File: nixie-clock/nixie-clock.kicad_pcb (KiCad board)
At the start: 2 copper layers, 57 parts, among them J1 Barrel_Jack_Switch, J2 Conn_01x08, J3 Conn_01x06, J4 AVR-ISP-6, U1 NCH6100HV, U10 74HC595, U11 74141, U12 74141, U2 ATmega328P-PU, U3 Mini360_Buck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

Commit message: Placed parts on board in approximate final locations. Created trace breakout for nixie tubes.
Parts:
- removed the REF** at (269.0, 39.0)
- removed the REF** at (254.0, 32.0)
- removed the REF** at (245.0, 37.0)
- removed the REF** at (257.0, 43.0)
- added REF**: MountingHole_2.7mm_M2.5_Pad, MountingHole:MountingHole_2.7mm_M2.5_Pad, F.Cu at (231.0, 46.0)
- added REF**: MountingHole_2.7mm_M2.5_Pad, MountingHole:MountingHole_2.7mm_M2.5_Pad, F.Cu at (240.0, 46.0)
- added REF**: MountingHole_2.7mm_M2.5_Pad, MountingHole:MountingHole_2.7mm_M2.5_Pad, F.Cu at (240.0, 38.0)
- added REF**: MountingHole_2.7mm_M2.5_Pad, MountingHole:MountingHole_2.7mm_M2.5_Pad, F.Cu at (231.0, 54.0)
- moved REF** 213.8 mm to (32.0, 34.0)
- moved N7 150.1 mm to (166.0, 103.0), turned to 180 degrees
- moved R11 137.3 mm to (79.0, 58.5), turned to 270 degrees
- moved R12 130.6 mm to (69.0, 58.5), turned to 270 degrees
- moved R13 127.5 mm to (64.0, 58.5), turned to 270 degrees
- moved R10 126.7 mm to (84.0, 58.5), turned to 270 degrees
- moved R14 126.2 mm to (54.0, 58.5), turned to 270 degrees
- moved R3 122.0 mm to (59.0, 58.5), turned to 270 degrees
- moved R2 120.8 mm to (74.0, 58.5), turned to 270 degrees
- moved R15 119.7 mm to (49.0, 58.5), turned to 270 degrees
- moved N8 114.9 mm to (114.0, 103.0), turned to 180 degrees
- moved C9 103.2 mm to (50.0, 80.0), turned to 90 degrees
- moved U12 100.9 mm to (72.0, 86.0)
- moved U10 97.5 mm to (72.0, 74.0)
- moved J3 90.2 mm to (94.0, 49.0), turned to 180 degrees
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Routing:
- net Net-(N6-Pad1): track 0.00 -> 50.9 mm
- net Net-(N5-Pad1): track 0.00 -> 50.9 mm
- net Net-(N6-Pad0): track 0.00 -> 42.0 mm
- net Net-(N5-Pad0): track 0.00 -> 42.0 mm
- net Net-(N6-Pad2): track 0.00 -> 41.9 mm
- net Net-(N5-Pad2): track 0.00 -> 41.9 mm
- net Net-(N6-Pad3): track 0.00 -> 31.9 mm
- net Net-(N5-Pad3): track 0.00 -> 31.9 mm
- net Net-(N6-Pad9): track 0.00 -> 31.5 mm
- net Net-(N5-Pad9): track 0.00 -> 31.5 mm
- net Net-(N4-Pad1): track 0.00 -> 26.5 mm
- net Net-(N3-Pad1): track 0.00 -> 26.5 mm
- net Net-(N6-Pad8): track 0.00 -> 24.4 mm
- net Net-(N5-Pad8): track 0.00 -> 24.4 mm
- net Net-(N2-Pad1): track 0.00 -> 22.7 mm
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- added copper zone on F.Cu, net +5V
- added copper zone on B.Cu, net GND
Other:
- board outline added: 184 x 112 mm
- net class Default: via_dia 0.8 -> 0.381; via_drill 0.4 -> 0.254
- rule via_min_size: 0.3 -> 0.381

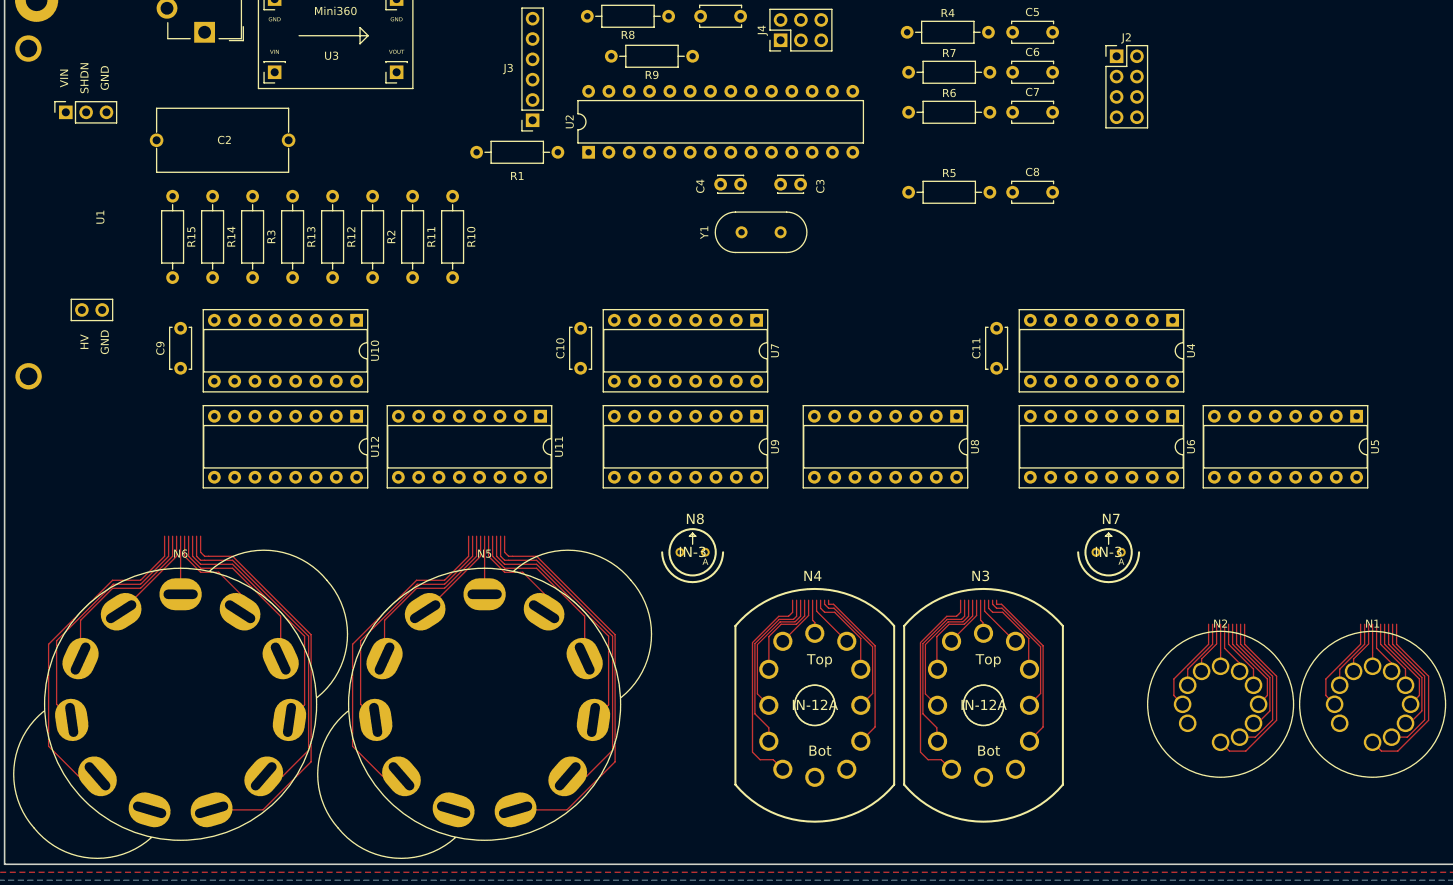
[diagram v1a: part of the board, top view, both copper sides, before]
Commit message: Readded pushbuttons to mainboard as an option. Beginning K155ID1-nixie exchange zone.
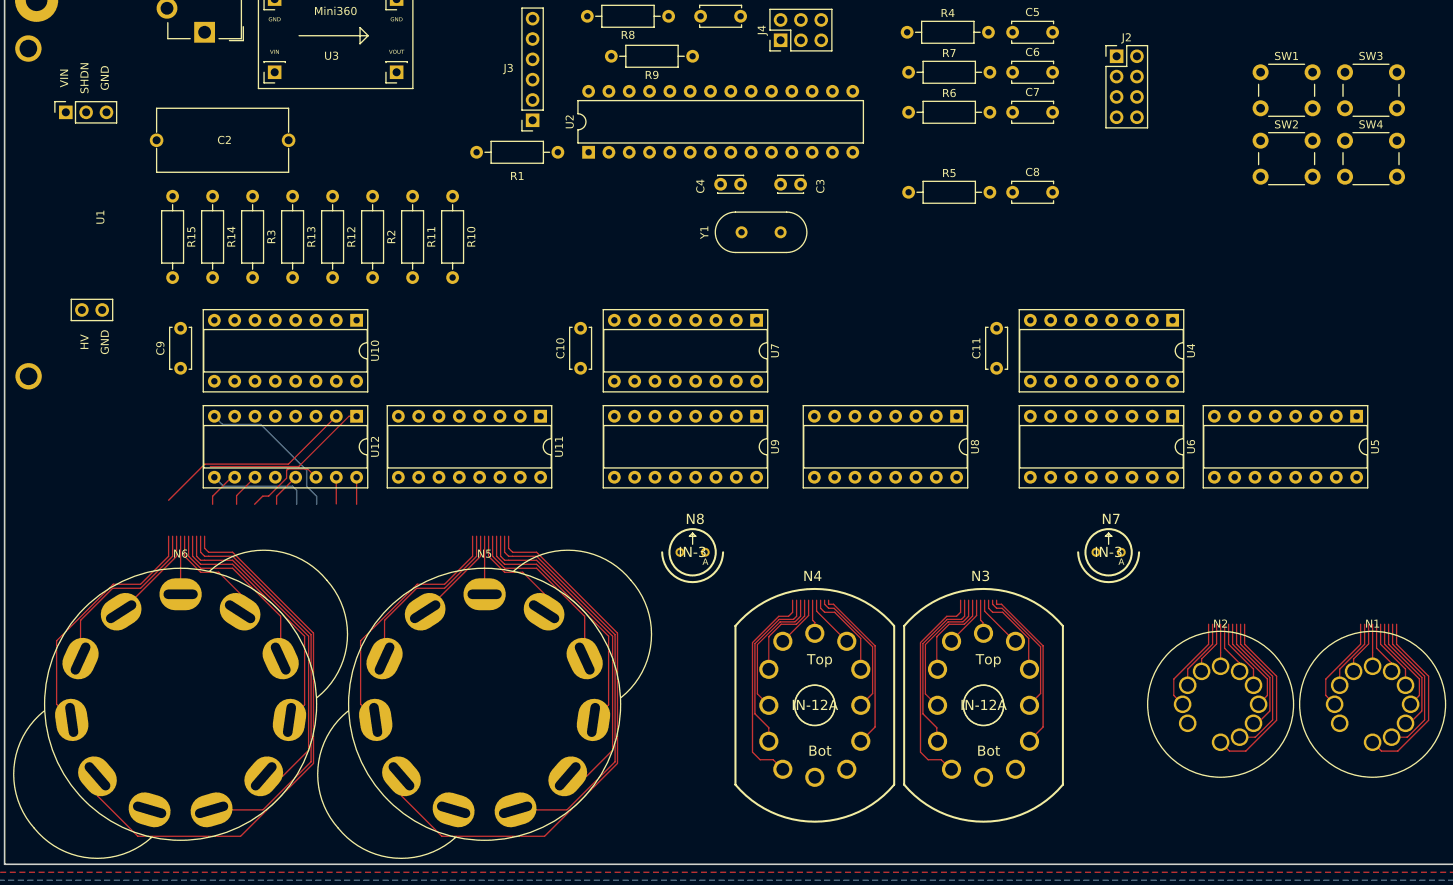
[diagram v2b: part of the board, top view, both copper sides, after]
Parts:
- added SW1: SW_Push, Button_Switch_THT:SW_PUSH_6mm, F.Cu at (185.0, 43.0)
- added SW2: SW_Push, Button_Switch_THT:SW_PUSH_6mm, F.Cu at (185.0, 51.5)
- added SW3: SW_Push, Button_Switch_THT:SW_PUSH_6mm, F.Cu at (195.6, 43.0)
- added SW4: SW_Push, Button_Switch_THT:SW_PUSH_6mm, F.Cu at (195.6, 51.5)
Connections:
- net Net-(N1-Pad0) renamed /shiftout/N1_0
- net Net-(N1-Pad1) renamed /shiftout/N1_1
- net Net-(N1-Pad2) renamed /shiftout/N1_2
- net Net-(N1-Pad3) renamed /shiftout/N1_3
- net Net-(N1-Pad4) renamed /shiftout/N1_4
- net Net-(N1-Pad5) renamed /shiftout/N1_5
- net Net-(N1-Pad6) renamed /shiftout/N1_6
- net Net-(N1-Pad7) renamed /shiftout/N1_7
- net Net-(N1-Pad8) renamed /shiftout/N1_8
- net Net-(N1-Pad9) renamed /shiftout/N1_9
- net Net-(N2-Pad0) renamed /shiftout/N2_0
- net Net-(N2-Pad1) renamed /shiftout/N2_1
- net Net-(N2-Pad2) renamed /shiftout/N2_2
- net Net-(N2-Pad3) renamed /shiftout/N2_3
- net Net-(N2-Pad4) renamed /shiftout/N2_4
- net Net-(N2-Pad5) renamed /shiftout/N2_5
- net Net-(N2-Pad6) renamed /shiftout/N2_6
- net Net-(N2-Pad7) renamed /shiftout/N2_7
- net Net-(N2-Pad8) renamed /shiftout/N2_8
- net Net-(N2-Pad9) renamed /shiftout/N2_9
- net Net-(N3-Pad0) renamed /shiftout/N3_0
- net Net-(N3-Pad1) renamed /shiftout/N3_1
- net Net-(N3-Pad2) renamed /shiftout/N3_2
- net Net-(N3-Pad3) renamed /shiftout/N3_3
- net Net-(N3-Pad4) renamed /shiftout/N3_4
- net Net-(N3-Pad5) renamed /shiftout/N3_5
- net Net-(N3-Pad6) renamed /shiftout/N3_6
- net Net-(N3-Pad7) renamed /shiftout/N3_7
- net Net-(N3-Pad8) renamed /shiftout/N3_8
- net Net-(N3-Pad9) renamed /shiftout/N3_9
- net Net-(N4-Pad0) renamed /shiftout/N4_0
- net Net-(N4-Pad1) renamed /shiftout/N4_1
- net Net-(N4-Pad2) renamed /shiftout/N4_2
- net Net-(N4-Pad3) renamed /shiftout/N4_3
- net Net-(N4-Pad4) renamed /shiftout/N4_4
- net Net-(N4-Pad5) renamed /shiftout/N4_5
- net Net-(N4-Pad6) renamed /shiftout/N4_6
- net Net-(N4-Pad7) renamed /shiftout/N4_7
- net Net-(N4-Pad8) renamed /shiftout/N4_8
- net Net-(N4-Pad9) renamed /shiftout/N4_9
- net Net-(N5-Pad0) renamed /shiftout/N5_0
- net Net-(N5-Pad1) renamed /shiftout/N5_1
- net Net-(N5-Pad2) renamed /shiftout/N5_2
- net Net-(N5-Pad3) renamed /shiftout/N5_3
- net Net-(N5-Pad4) renamed /shiftout/N5_4
- net Net-(N5-Pad5) renamed /shiftout/N5_5
- net Net-(N5-Pad6) renamed /shiftout/N5_6
- net Net-(N5-Pad7) renamed /shiftout/N5_7
- net Net-(N5-Pad8) renamed /shiftout/N5_8
- net Net-(N5-Pad9) renamed /shiftout/N5_9
- net Net-(N6-Pad0) renamed /shiftout/N6_0
- net Net-(N6-Pad1) renamed /shiftout/N6_1
- net Net-(N6-Pad2) renamed /shiftout/N6_2
- net Net-(N6-Pad3) renamed /shiftout/N6_3
- net Net-(N6-Pad4) renamed /shiftout/N6_4
- net Net-(N6-Pad5) renamed /shiftout/N6_5
- net Net-(N6-Pad6) renamed /shiftout/N6_6
- net Net-(N6-Pad7) renamed /shiftout/N6_7
- net Net-(N6-Pad8) renamed /shiftout/N6_8
- net Net-(N6-Pad9) renamed /shiftout/N6_9
- net Net-(U10-Pad1) renamed /shiftout/N5_B
- net Net-(U10-Pad15) renamed /shiftout/N5_A
- net Net-(U10-Pad2) renamed /shiftout/N5_C
- net Net-(U10-Pad3) renamed /shiftout/N5_D
- net Net-(U10-Pad4) renamed /shiftout/N6_A
- net Net-(U10-Pad5) renamed /shiftout/N6_B
- net Net-(U10-Pad6) renamed /shiftout/N6_C
- net Net-(U10-Pad7) renamed /shiftout/N6_D
- net Net-(U4-Pad1) renamed /shiftout/N1_B
- net Net-(U4-Pad15) renamed /shiftout/N1_A
- net Net-(U4-Pad2) renamed /shiftout/N1_C
- net Net-(U4-Pad3) renamed /shiftout/N1_D
- net Net-(U4-Pad4) renamed /shiftout/N2_A
- net Net-(U4-Pad5) renamed /shiftout/N2_B
- net Net-(U4-Pad6) renamed /shiftout/N2_C
- net Net-(U4-Pad7) renamed /shiftout/N2_D
- net Net-(U7-Pad1) renamed /shiftout/N3_B
- net Net-(U7-Pad15) renamed /shiftout/N3_A
- net Net-(U7-Pad2) renamed /shiftout/N3_C
- net Net-(U7-Pad3) renamed /shiftout/N3_D
- net Net-(U7-Pad4) renamed /shiftout/N4_A
- net Net-(U7-Pad5) renamed /shiftout/N4_B
- net Net-(U7-Pad6) renamed /shiftout/N4_C
- net Net-(U7-Pad7) renamed /shiftout/N4_D
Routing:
- net /shiftout/N6_0: track 42.0 -> 74.5 mm
- net /shiftout/N5_0: track 42.0 -> 68.7 mm
- net /shiftout/N6_9: track 31.5 -> 56.9 mm
- net /shiftout/N6_8: track 24.4 -> 45.3 mm
- net /shiftout/N6_2: track 41.9 -> 60.9 mm
- net /shiftout/N6_3: track 31.9 -> 44.6 mm
- net /shiftout/N6_5: track 13.6 -> 24.1 mm
- net /shiftout/N6_7: track 12.3 -> 17.1 mm
- net /shiftout/N6_4: track 22.4 -> 26.8 mm
- net /shiftout/N6_6: track 7.25 -> 11.6 mm
- net /shiftout/N6_1: track 50.9 -> 54.2 mm

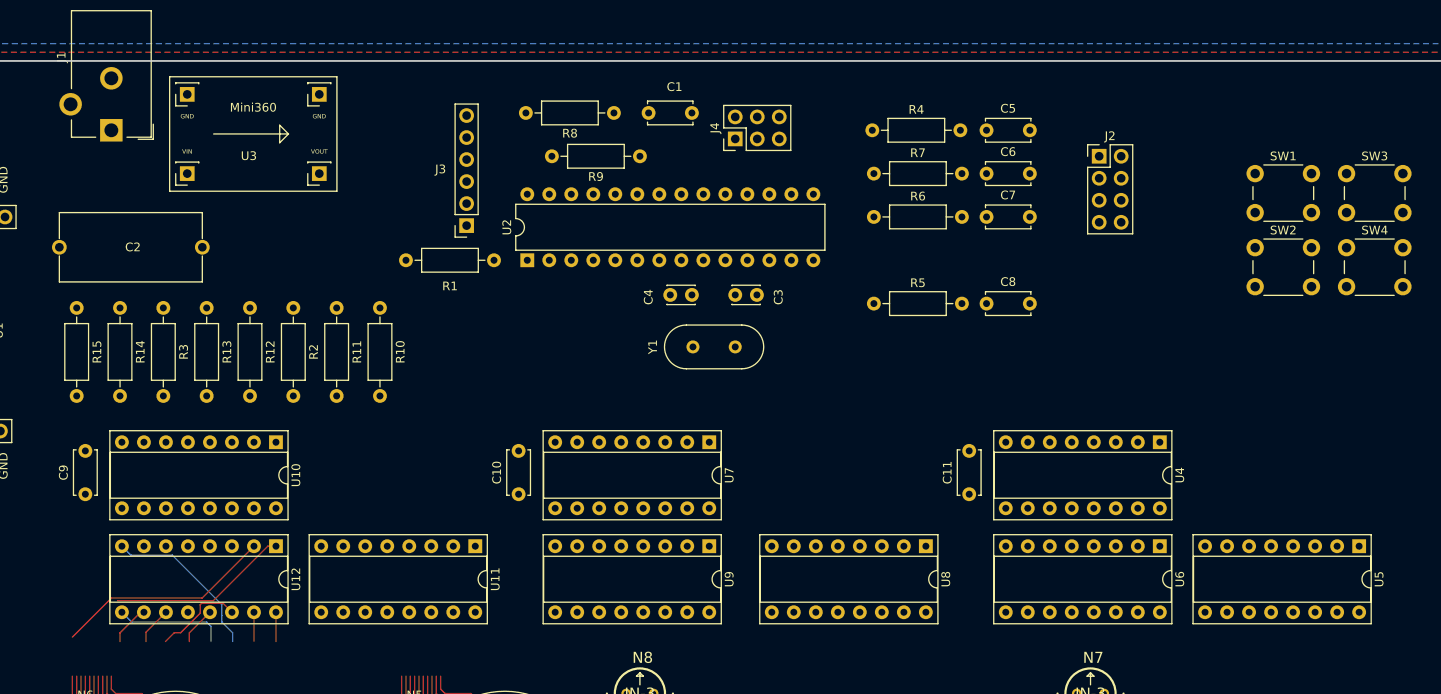
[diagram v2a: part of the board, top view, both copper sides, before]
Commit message: Both sides of exchange zone ready for connecting for IN-1, IN-2. Discovered IN-12 has reverse order so will need to redo traces for the K155ID1s attached to those nixies.
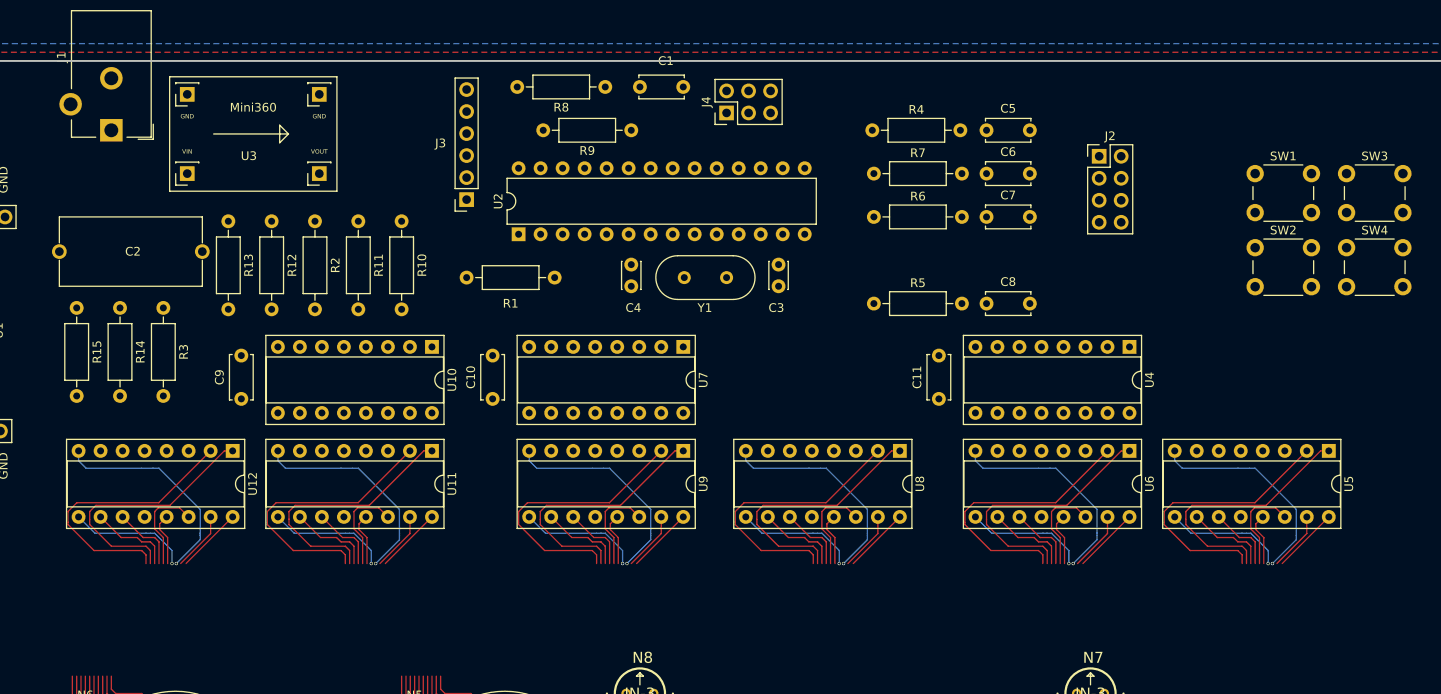
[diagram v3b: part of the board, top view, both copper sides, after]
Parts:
- moved C9 21.1 mm to (68.0, 69.0)
- moved U10 21.1 mm to (90.0, 63.0)
- moved U11 12.1 mm to (90.0, 75.0)
- moved U12 12.1 mm to (67.0, 75.0)
- moved C11 11.5 mm to (148.5, 69.0)
- moved U4 11.5 mm to (170.5, 63.0)
- moved U5 11.5 mm to (193.5, 75.0)
- moved U6 11.5 mm to (170.5, 75.0)
- moved C10 11.4 mm to (97.0, 69.0)
- moved U7 11.4 mm to (119.0, 63.0)
- moved U8 11.4 mm to (144.0, 75.0)
- moved U9 11.4 mm to (119.0, 75.0)
- moved R10 10.3 mm to (86.5, 48.5)
- moved R11 10.3 mm to (81.5, 48.5)
- moved R12 10.3 mm to (71.5, 48.5)
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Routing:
- net /shiftout/N3_9: track 16.6 -> 48.9 mm
- net /shiftout/N5_9: track 31.5 -> 63.9 mm
- net /shiftout/N4_9: track 16.6 -> 48.9 mm
- net /shiftout/N2_9: track 8.91 -> 41.2 mm
- net /shiftout/N1_9: track 8.91 -> 41.2 mm
- net /shiftout/N5_8: track 24.4 -> 55.0 mm
- net /shiftout/N3_8: track 11.4 -> 42.1 mm
- net /shiftout/N2_8: track 6.66 -> 37.3 mm
- net /shiftout/N1_8: track 6.66 -> 37.3 mm
- net /shiftout/N4_8: track 11.4 -> 42.1 mm
- net /shiftout/N4_2: track 21.6 -> 46.4 mm, vias 0 -> 1
- net /shiftout/N3_2: track 21.6 -> 46.4 mm, vias 0 -> 1
- net /shiftout/N2_2: track 18.6 -> 43.5 mm, vias 0 -> 1
- net /shiftout/N1_2: track 18.6 -> 43.5 mm, vias 0 -> 1
- net /shiftout/N5_2: track 41.9 -> 66.7 mm, vias 0 -> 1
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
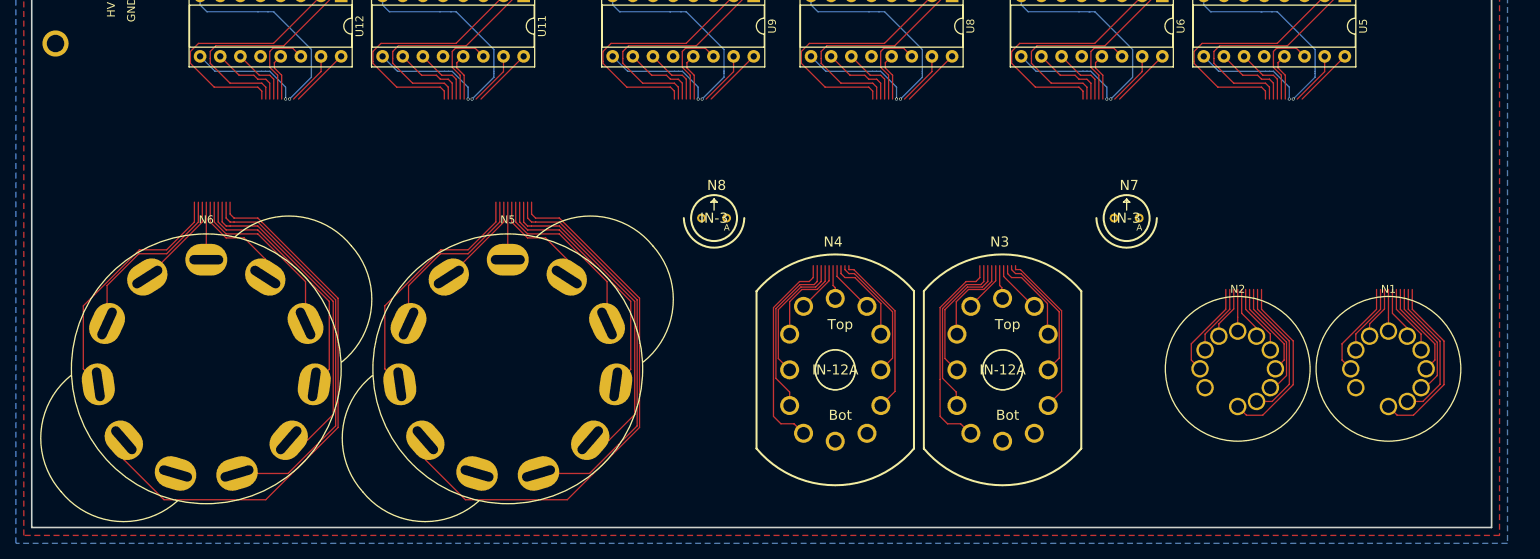
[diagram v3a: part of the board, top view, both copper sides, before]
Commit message: Finished K155ID1-nixie exchange zone routing.
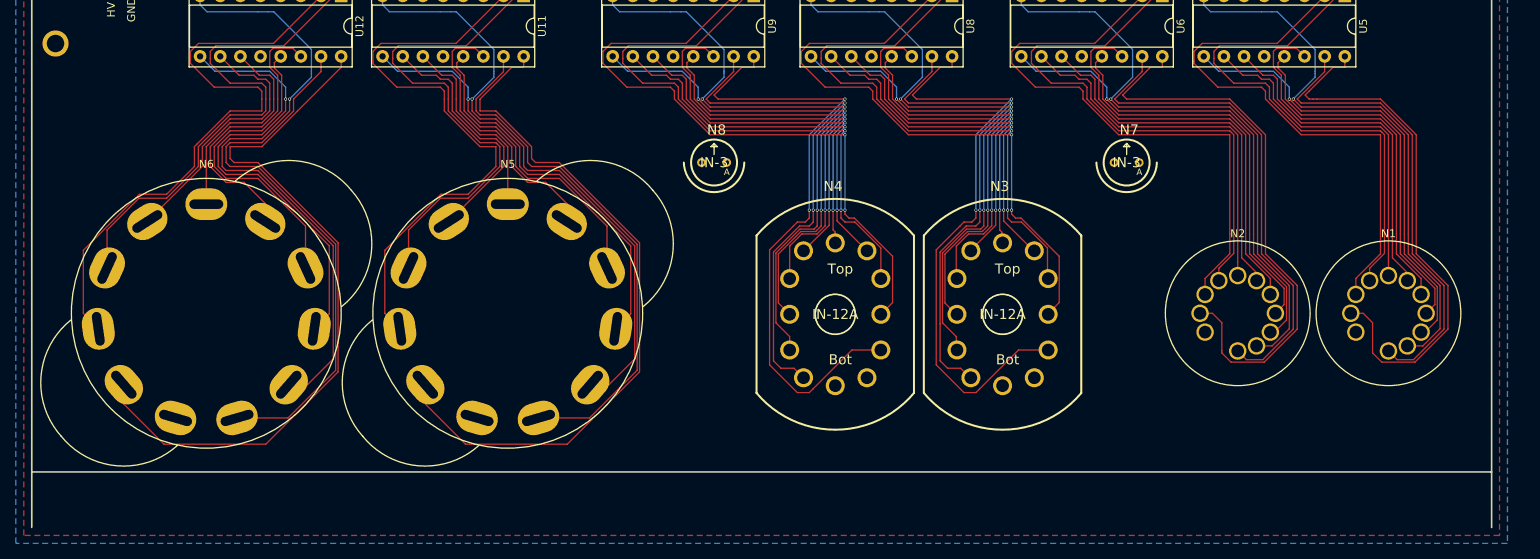
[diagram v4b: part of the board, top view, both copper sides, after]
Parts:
- moved N1 7.00 mm to (199.0, 115.0)
- moved N2 7.00 mm to (180.0, 115.0)
- moved N3 7.00 mm to (150.4, 115.1)
- moved N4 7.00 mm to (129.3, 115.1)
- moved N5 7.00 mm to (88.0, 115.0)
- moved N6 7.00 mm to (50.0, 115.0)
- moved N7 7.00 mm to (166.0, 96.0)
- moved N8 7.00 mm to (114.0, 96.0)
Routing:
- net /shiftout/N2_0: track 19.9 -> 72.8 mm
- net /shiftout/N4_0: track 28.7 -> 80.3 mm, vias 0 -> 2
- net /shiftout/N1_0: track 19.9 -> 68.8 mm
- net /shiftout/N3_0: track 28.7 -> 76.3 mm, vias 0 -> 2
- net /shiftout/N4_3: track 30.9 -> 63.8 mm, vias 1 -> 3
- net /shiftout/N4_6: track 12.1 -> 45.0 mm, vias 0 -> 2
- net /shiftout/N2_3: track 29.1 -> 62.0 mm
- net /shiftout/N4_8: track 42.1 -> 75.0 mm, vias 0 -> 2
- net /shiftout/N4_5: track 17.4 -> 50.3 mm, vias 0 -> 2
- net /shiftout/N2_9: track 41.2 -> 74.1 mm
- net /shiftout/N2_4: track 18.3 -> 51.2 mm
- net /shiftout/N2_2: track 43.5 -> 76.4 mm
- net /shiftout/N2_1: track 29.5 -> 62.4 mm
- net /shiftout/N4_7: track 16.3 -> 49.2 mm, vias 0 -> 2
- net /shiftout/N2_8: track 37.3 -> 70.2 mm
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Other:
- outline, holes or cut-outs redrawn
